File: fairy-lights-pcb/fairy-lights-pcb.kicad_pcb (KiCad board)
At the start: 2 copper layers, 60 x 60 mm, 16 parts, among them J1 Power_Jack, J2 Conn_LED_Strand, J3 Conn_LED_Strand, J4 Conn_Misc, J5 Conn_02x04_Top_Bottom, SW1 SW_PWR, SW2 SW_User, U1 WeMos_D1_mini, U2 TXS0108EPW

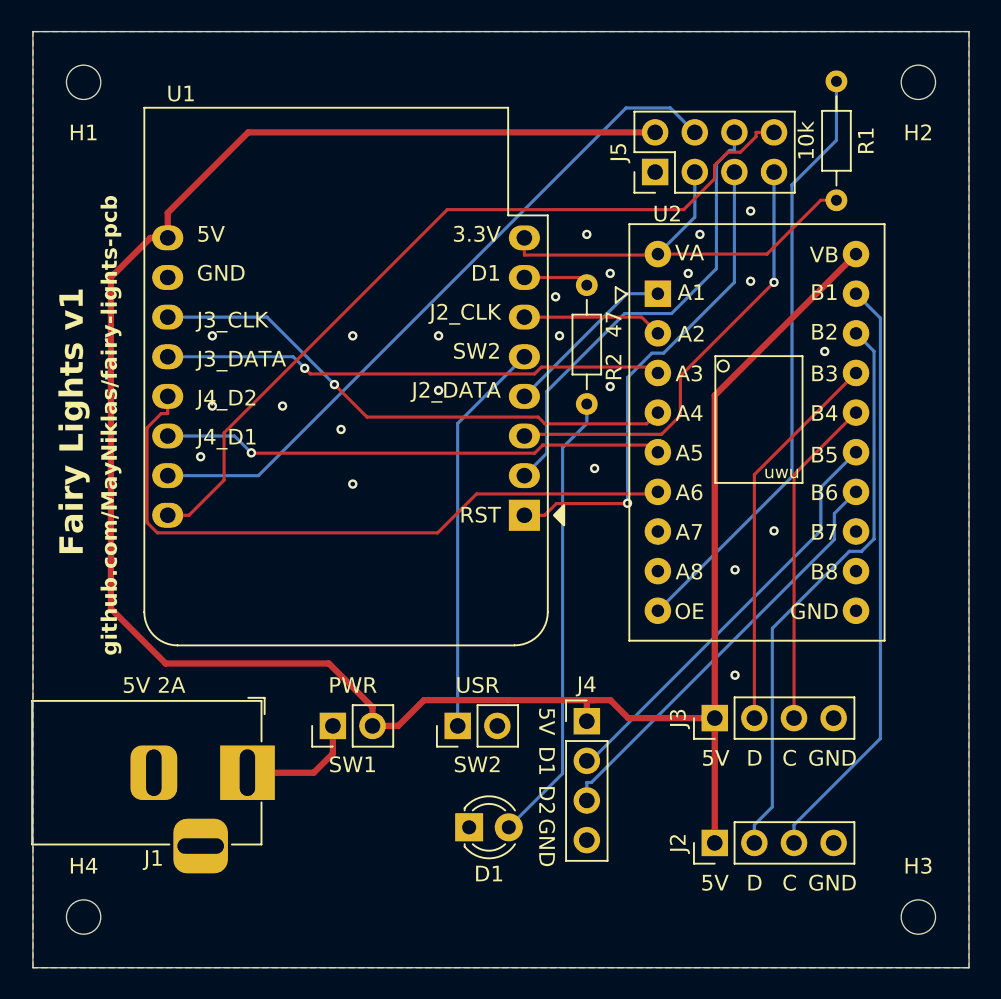
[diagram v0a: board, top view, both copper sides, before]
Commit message: Make room for power switch
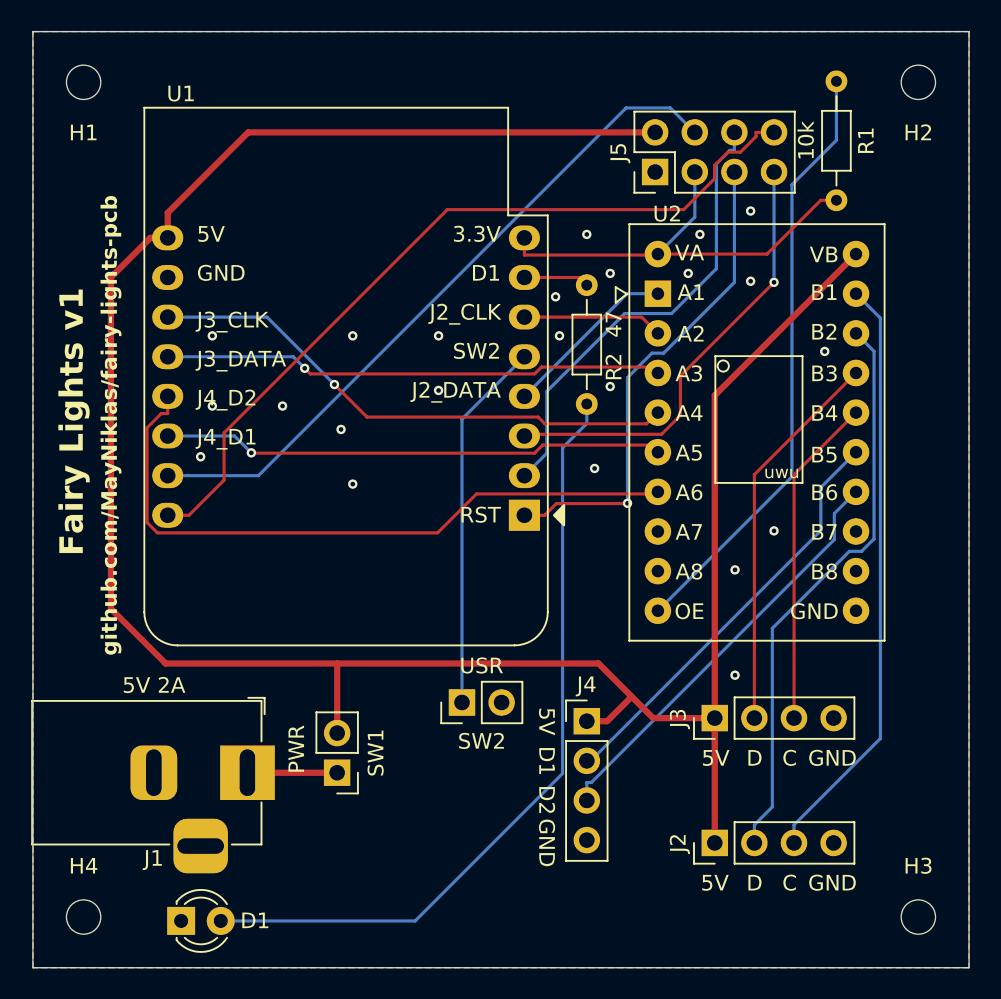
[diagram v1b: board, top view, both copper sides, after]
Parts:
- moved D1 19.4 mm to (69.5, 117.0)
- moved SW1 3.01 mm to (79.5, 107.5), turned to 180 degrees
- moved SW2 1.53 mm to (87.5, 103.0)
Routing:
- net Net-(D1-A): track 29.2 -> 50.1 mm
- net +5V: track 147.9 -> 152.0 mm
- net /5V_RAW: track 7.76 -> 5.75 mm
- net Net-(U1-MISO/D6): track 25.4 -> 23.8 mm

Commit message: Update pins and labels
- All MCU pin silkscreen labels should now be correct.
- The board title is updated to say "r(evision)" instead of "v(ersion)".
- The middle pins of J3 and J4 are swapped for totally valid reasons
  (viz. schematic symmetry).
- J4 is turned into a LED strand connector (such that its pin labels
  match the I2C functions of the corresponding MCU pins).
- Traces are rerouted to account for the schematic changes and to reduce
  ugly spots.
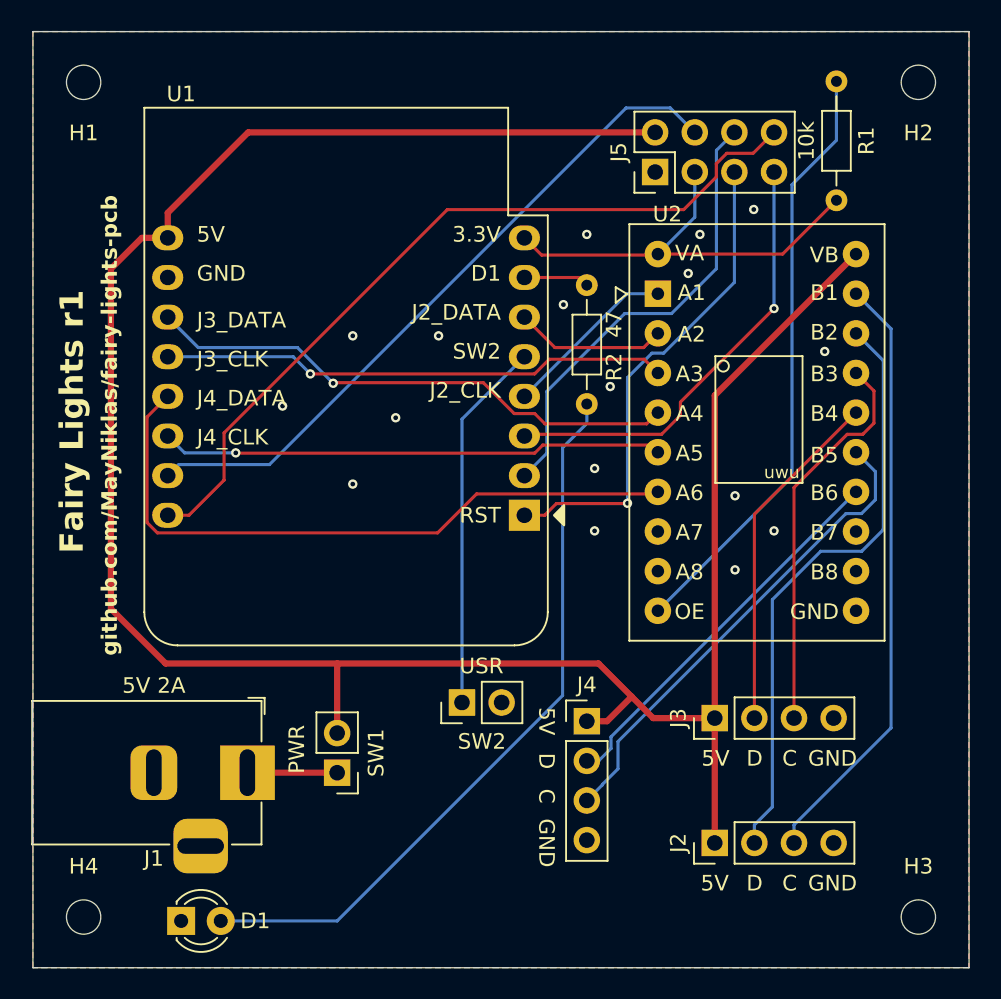
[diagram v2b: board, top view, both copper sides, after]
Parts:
- J4: value Conn_Misc -> Conn_LED_Strand
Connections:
- U2 pad 14: Net-(J4-D2) -> Net-(J4-D1)
- U2 pad 15: Net-(J4-D1) -> Net-(J4-D2)
- U2 pad 16: Net-(J3-CLK) -> Net-(J3-DATA)
- U2 pad 17: Net-(J3-DATA) -> Net-(J3-CLK)
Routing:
- net Net-(J3-CLK): track 21.2 -> 25.3 mm
- net Net-(J4-D2): track 27.1 -> 31.1 mm
- net Net-(D1-A): track 50.1 -> 47.2 mm
- net Net-(J3-DATA): track 24.8 -> 22.3 mm
- net Net-(J4-D1): track 27.1 -> 24.8 mm
- net Net-(J2-DATA): track 36.8 -> 38.3 mm
- net Net-(U1-MOSI/D7): track 8.99 -> 9.74 mm
- net +3.3V: track 28.8 -> 28.2 mm
- net Net-(J2-CLK): track 38.1 -> 38.7 mm
- net GND: vias 23 -> 17
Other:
- board text added: "Fairy Lights r1"
- board text added: "J4_CLK"
- board text added: "J4_DATA"
- board text removed: "D2"
- board text removed: "Fairy Lights v1"
- board text removed: "J4_D1"
- board text removed: "J4_D2"

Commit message: Use different status LED
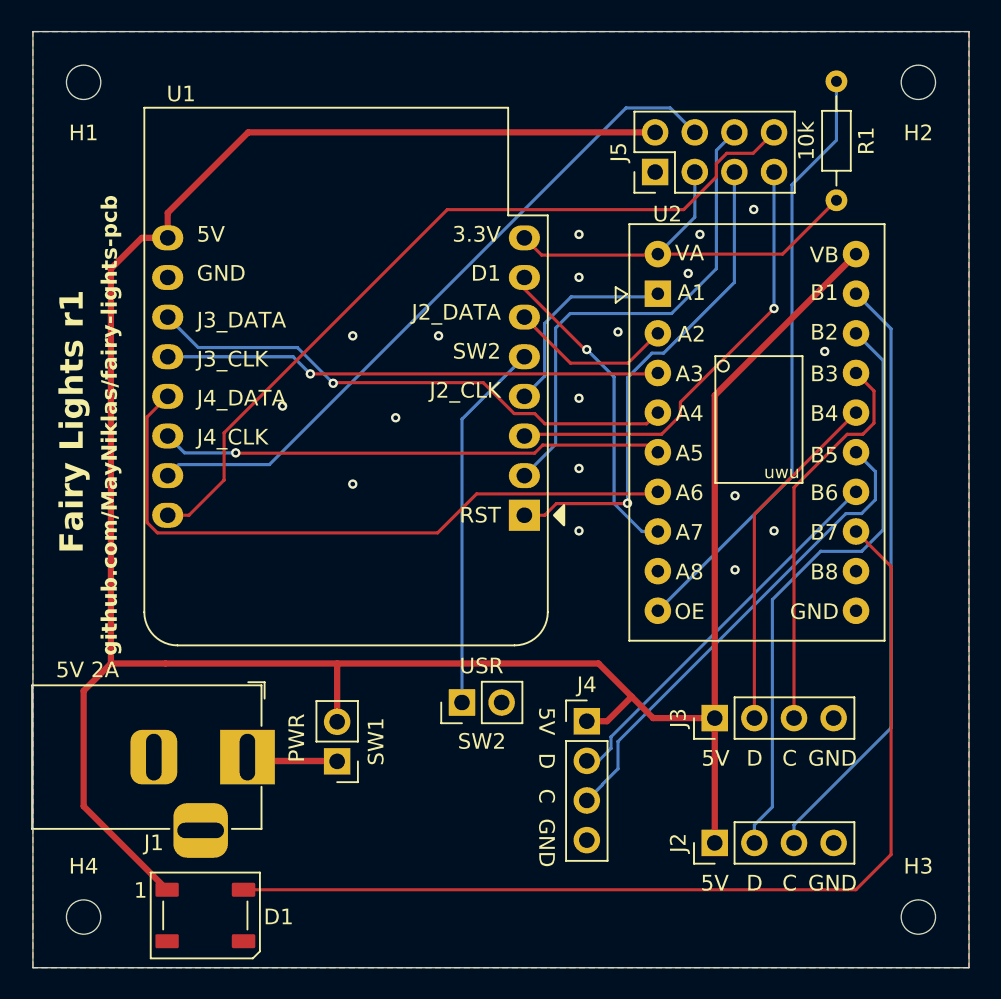
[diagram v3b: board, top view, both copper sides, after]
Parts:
- removed R2: 47, Resistor_THT:R_Axial_DIN0204_L3.6mm_D1.6mm_P7.62mm_Horizontal
- D1: value LED -> WS2812B; footprint LED_THT:LED_D3.0mm -> LED_SMD:LED_WS2812B_PLCC4_5.0x5.0mm_P3.2mm
- moved D1 1.59 mm to (71.0, 116.7)
- moved J1 1.00 mm to (73.8, 106.5)
- moved SW1 0.72 mm to (79.5, 106.8)
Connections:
- D1 pad 1: GND -> +5V
- D1 pad 2: Net-(D1-A) -> unconnected-(D1-DOUT-Pad2)
- U2 pad 13: unconnected-(U2-B7-Pad13) -> Net-(D1-DIN)
- U2 pad 8: unconnected-(U2-A7-Pad8) -> Net-(U1-CS/D8)
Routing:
- net Net-(D1-DIN): track 0.00 -> 64.1 mm
- net Net-(D1-A): track 47.2 -> 0.00 mm
- net +5V: track 152.3 -> 171.1 mm
- net Net-(U1-CS/D8): track 4.20 -> 20.5 mm, vias 0 -> 1
- net UC_A0: track 29.3 -> 31.4 mm
- net Net-(U1-SCK/D5): track 11.3 -> 13.3 mm
- net Net-(U1-MOSI/D7): track 9.74 -> 10.6 mm
- net Net-(U1-D3): track 32.6 -> 31.9 mm
- net GND: vias 17 -> 18

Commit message: Moar LEDs
We're also considering yeeting or replacing the level shifter. Until we
decide on what the replacement will be, I'll leave the current one in,
with the understanding that one could substitute a pin-compatible and
working replacement.
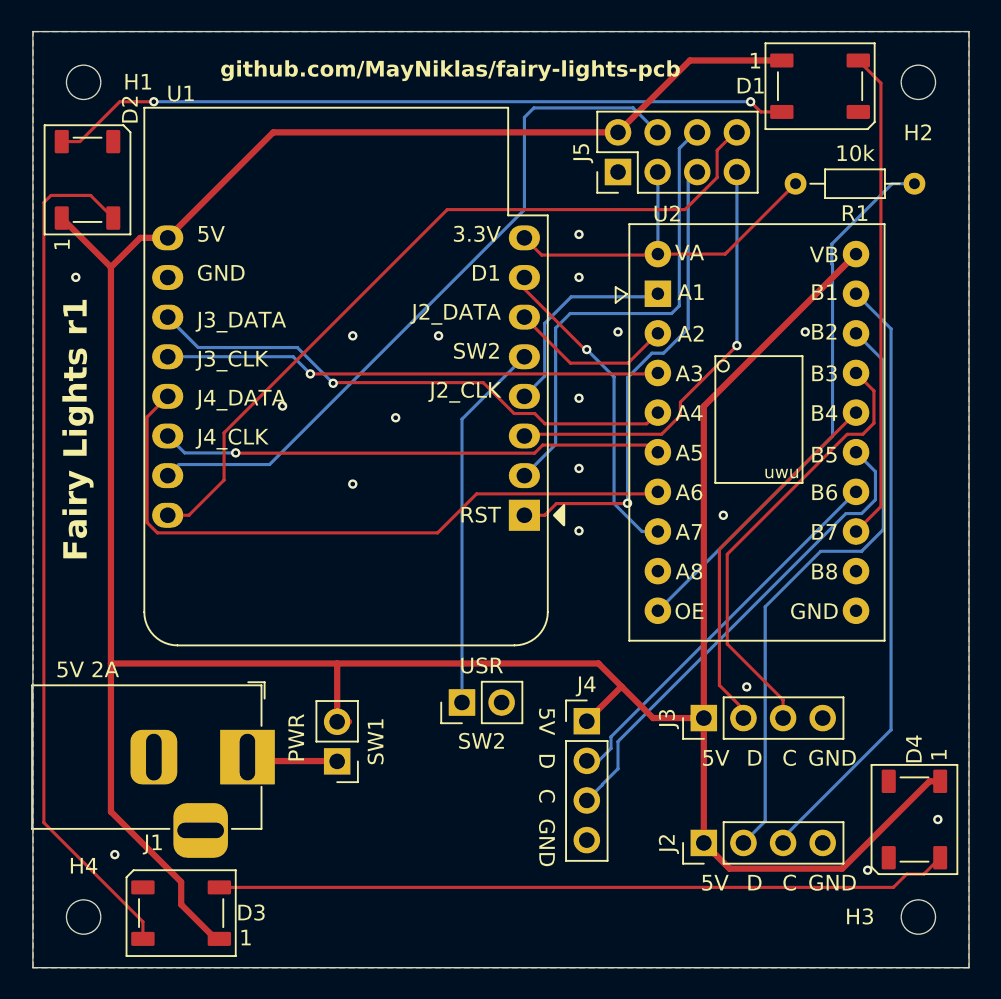
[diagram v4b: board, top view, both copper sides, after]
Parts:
- added D2: WS2812B, LED_SMD:LED_WS2812B_PLCC4_5.0x5.0mm_P3.2mm, F.Cu at (63.5, 69.5)
- added D3: WS2812B, LED_SMD:LED_WS2812B_PLCC4_5.0x5.0mm_P3.2mm, F.Cu at (69.5, 116.5)
- added D4: WS2812B, LED_SMD:LED_WS2812B_PLCC4_5.0x5.0mm_P3.2mm, F.Cu at (116.5, 110.5)
- moved D1 66.2 mm to (110.5, 63.5)
- moved R1 8.25 mm to (116.5, 69.8), turned to 180 degrees
- moved J5 2.38 mm to (97.5, 69.0)
- moved J2 0.70 mm to (103.0, 112.0)
- moved J3 0.70 mm to (103.0, 104.0)
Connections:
- D1 pad 2: unconnected-(D1-DOUT-Pad2) -> Net-(D1-DOUT)
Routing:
- net Net-(D2-DOUT): track 0.00 -> 55.1 mm
- net Net-(D1-DOUT): track 0.00 -> 47.5 mm, vias 0 -> 2
- net Net-(D3-DOUT): track 0.00 -> 47.0 mm
- net +5V: track 171.1 -> 205.3 mm
- net Net-(D1-DIN): track 64.1 -> 31.5 mm
- net Net-(U2-OE): track 38.7 -> 35.1 mm
- net Net-(J3-CLK): track 25.3 -> 28.6 mm
- net +3.3V: track 28.2 -> 25.0 mm
- net UC_TX: track 51.3 -> 49.4 mm
- net Net-(J3-DATA): track 22.3 -> 23.8 mm
- net UC_RX: track 44.2 -> 45.3 mm
- net UC_D0: track 28.6 -> 27.6 mm
- net UC_RST: track 31.4 -> 30.4 mm
- net UC_A0: track 31.4 -> 30.5 mm
